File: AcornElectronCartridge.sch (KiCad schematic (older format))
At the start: 5 parts

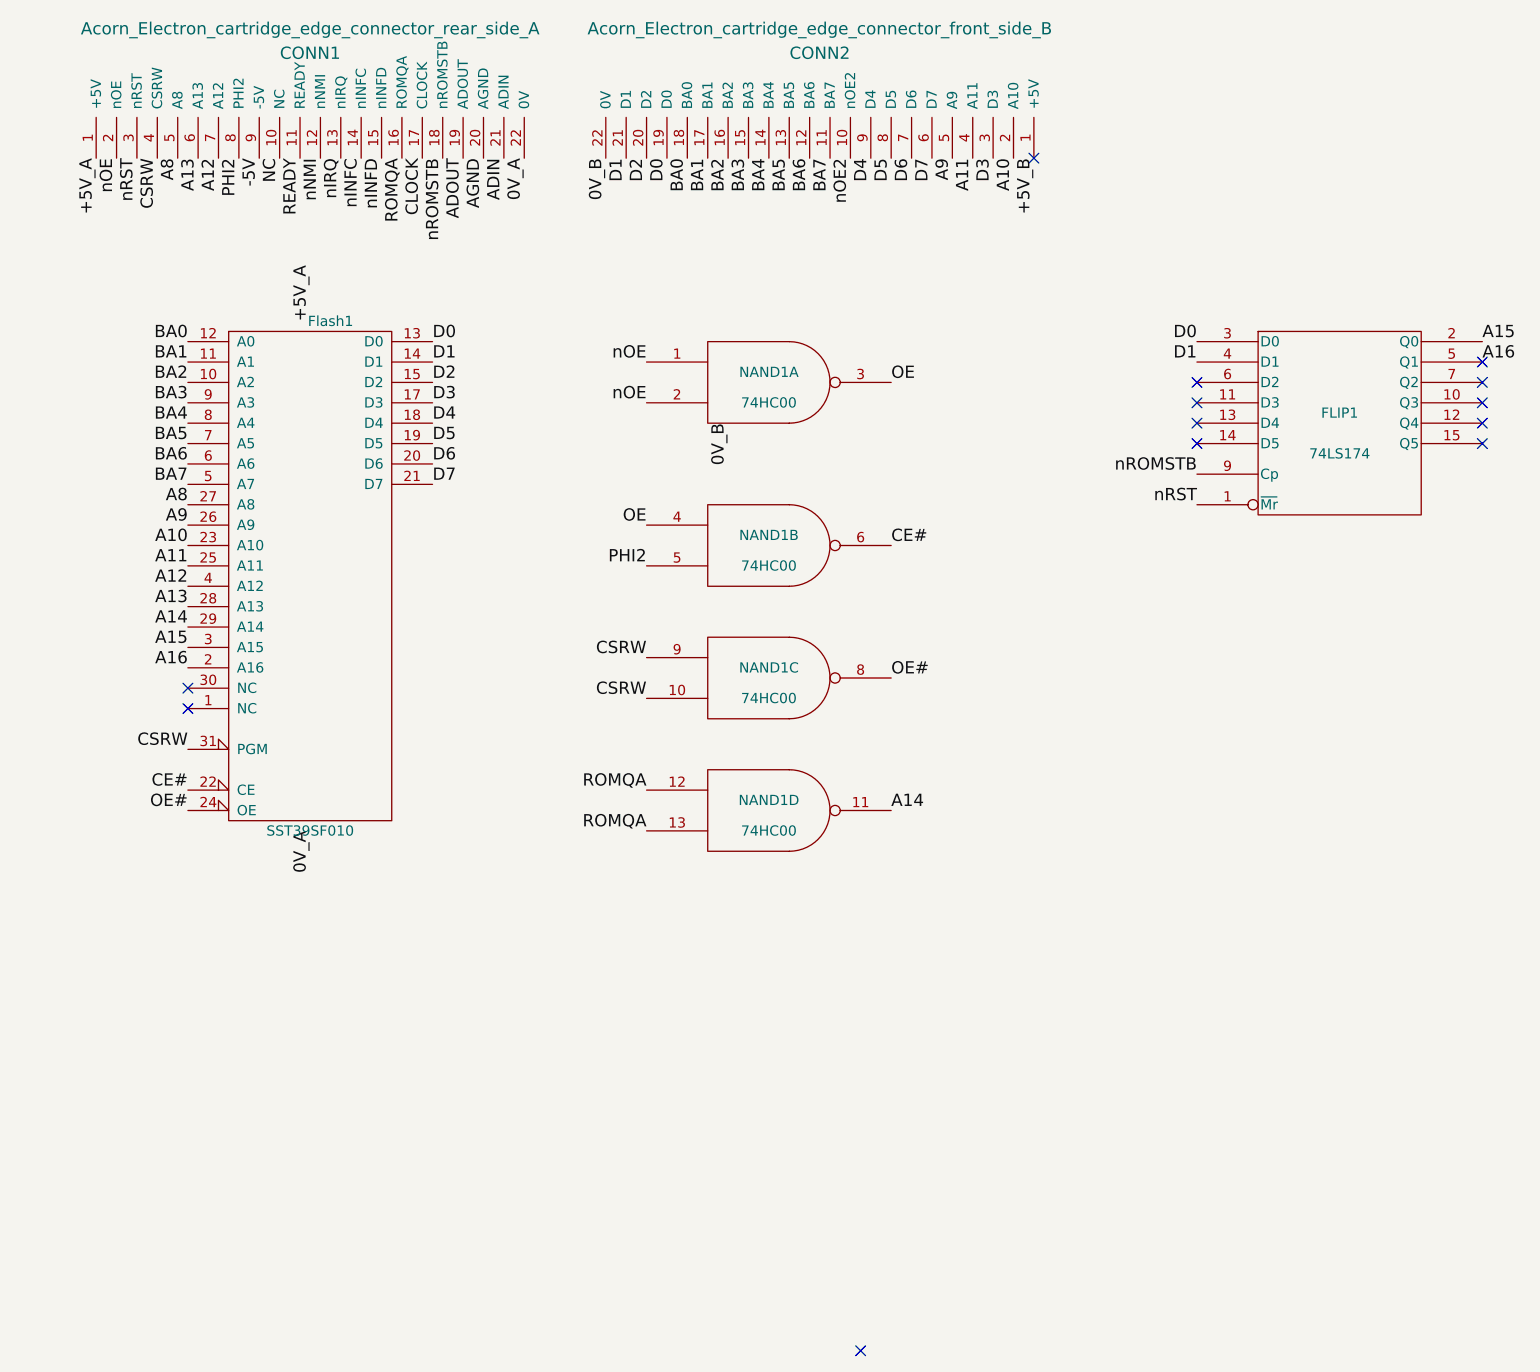
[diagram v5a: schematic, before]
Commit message: Placed all tracks linked to flash ROM pads on the same side of the board.
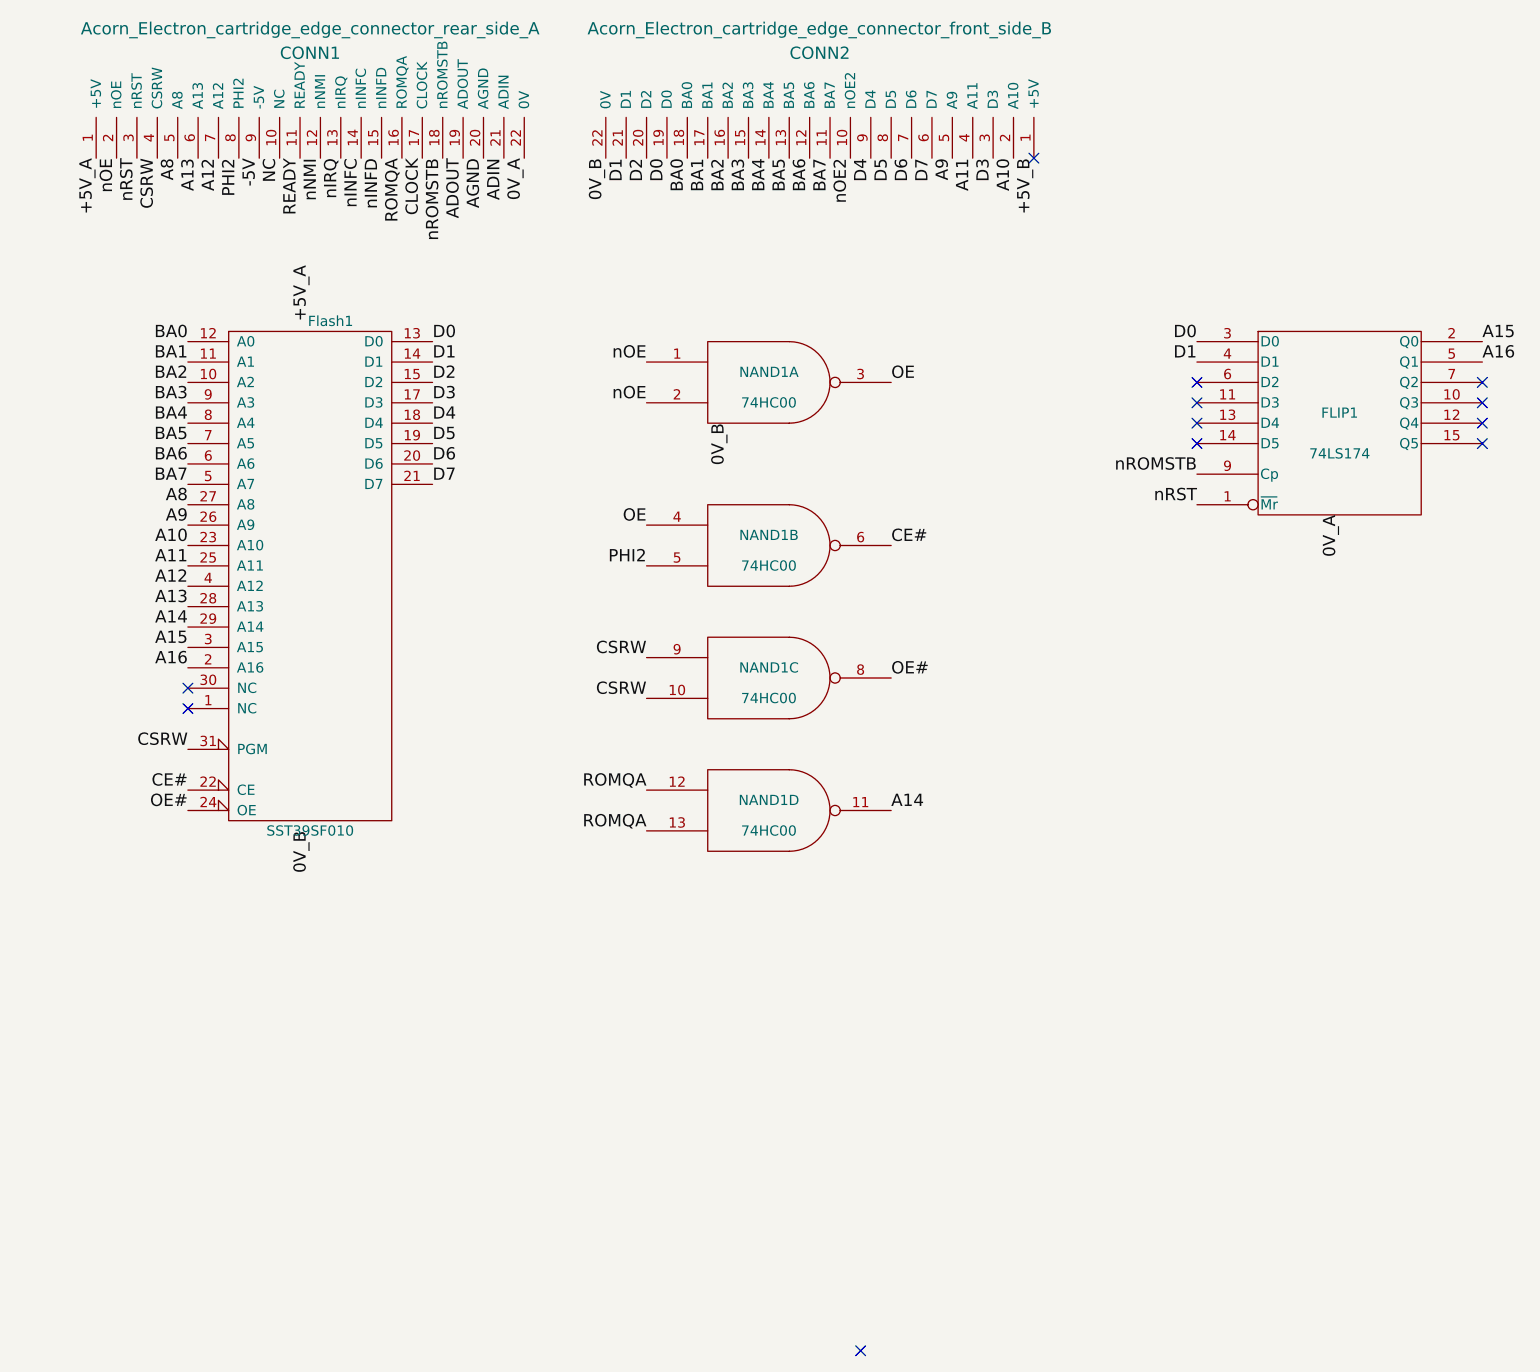
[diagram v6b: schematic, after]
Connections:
- no-connect marks 13 -> 12
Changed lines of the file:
@@
 Text Label 8500 2700 0    60   ~ 0
 A16
-NoConn ~ 8500 2700
 NoConn ~ 8500 2800
 NoConn ~ 8500 2900
@@
 0V_B
 Text Label 2750 5000 3    60   ~ 0
-0V_A
+0V_B
 Text Label 2750 2500 1    60   ~ 0
 +5V_A
+Text Label 7800 3450 3    60   ~ 0
+0V_A
 $EndSCHEMATC

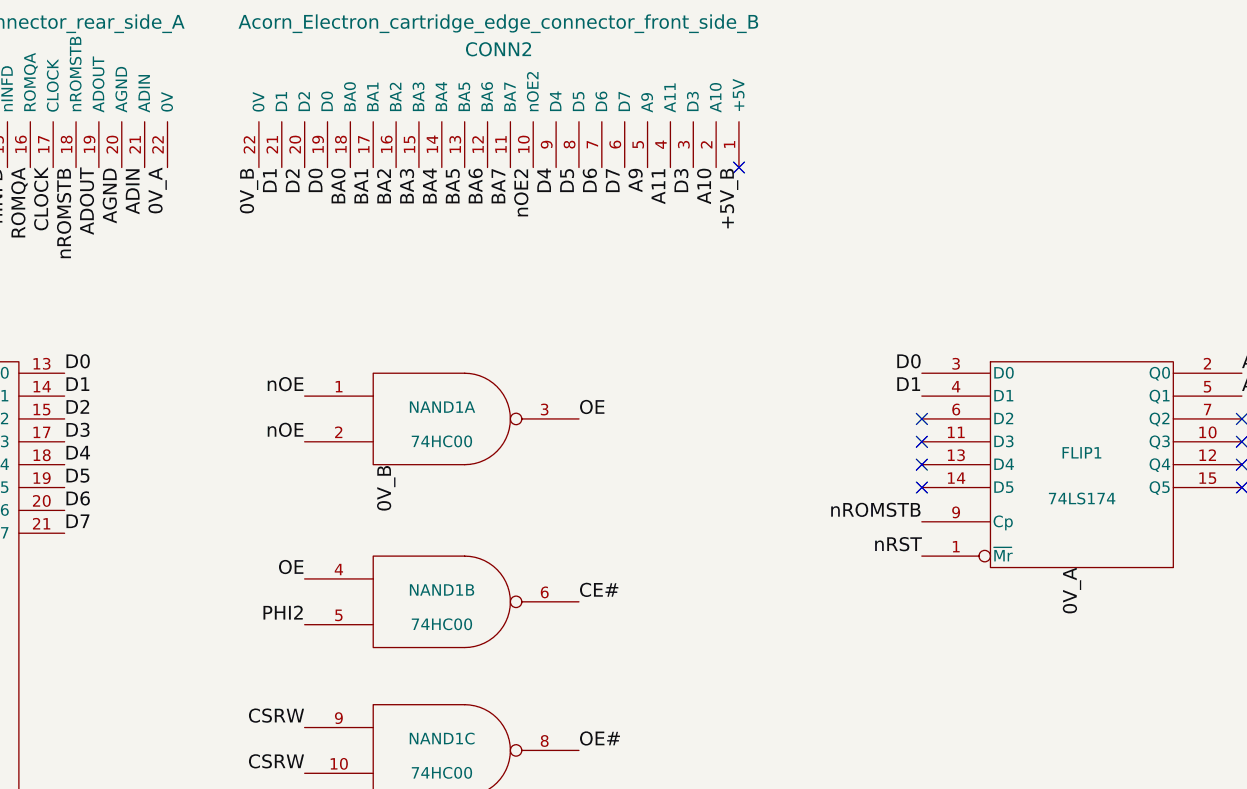
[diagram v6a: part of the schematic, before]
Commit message: Put all the chips on the same side of the board.
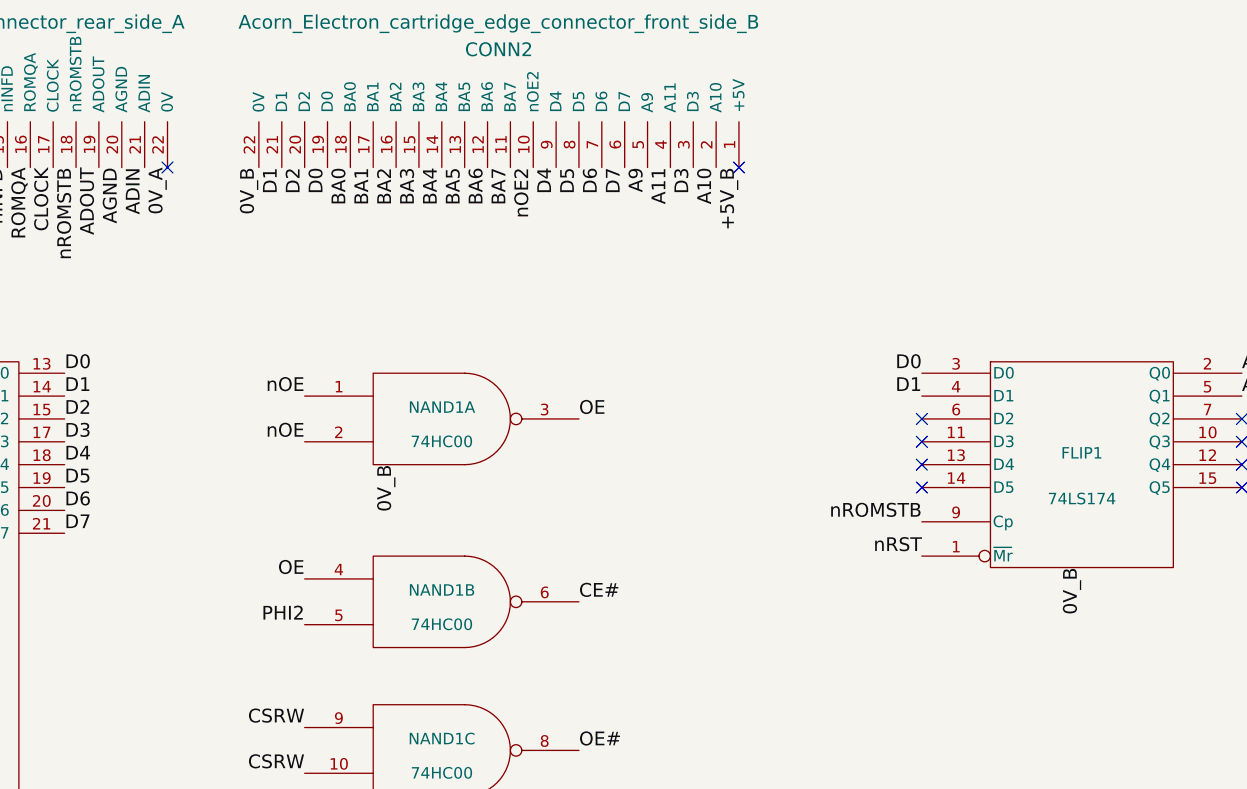
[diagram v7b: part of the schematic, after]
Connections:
- net GND: no longer CONN1.22 (0V)
- new net 0V_A: CONN1.22 (0V)
- no-connect marks 12 -> 13
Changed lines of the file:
@@
 A16
 NoConn ~ 6300 1700
-Text Label 4800 3000 3    60   ~ 0
+Text Label 2750 2500 1    60   ~ 0
++5V_A
+Text Label 7800 3450 3    60   ~ 0
 0V_B
 Text Label 2750 5000 3    60   ~ 0
 0V_B
-Text Label 2750 2500 1    60   ~ 0
-+5V_A
-Text Label 7800 3450 3    60   ~ 0
-0V_A
+NoConn ~ 3800 1700
+Text Label 4800 3000 3    60   ~ 0
+0V_B
 $EndSCHEMATC
